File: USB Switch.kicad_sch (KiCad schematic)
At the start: 2 parts

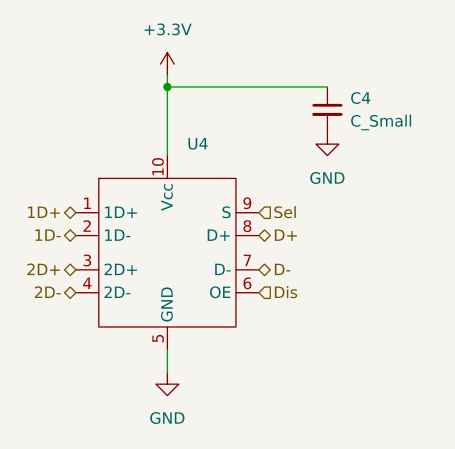
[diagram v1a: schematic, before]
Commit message: BMS updates
- BMS mostly done
- all BMS pins connected to RP2040
- Re-did Minibadge pinouts
- Connected RP2040 to USB Switch
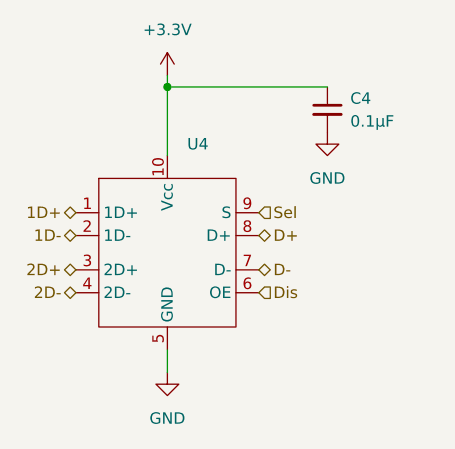
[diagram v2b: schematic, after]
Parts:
- C4: value C_Small -> 0.1μF
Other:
- company: (none) -> Pips Engineering
- title: (none) -> USB-C switch

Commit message: BMS updates
Added missing capacitor for OTG
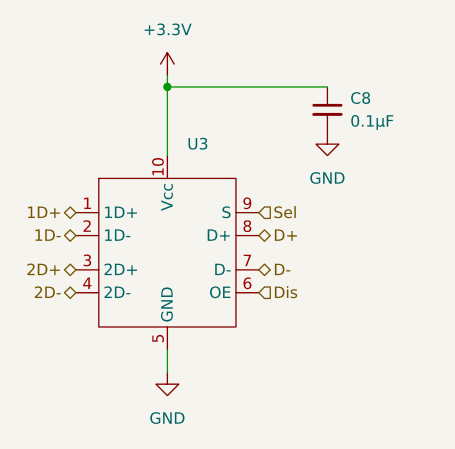
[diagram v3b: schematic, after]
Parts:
- renumbered C4 to C8, U4 to U3
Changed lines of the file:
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@@
 		(dnp no)
 		(fields_autoplaced yes)
-		(property "Reference" "#PWR0109"
+		(property "Reference" "#PWR026"
 			(at 162.56 81.28 0)
 			(effects
@@
 			(project "Minibadge Display 5x3"
 				(path "/e5119d15-74fb-4259-abbc-5cab1f368532/dd5131e2-5cc6-4770-9855-76714fa7cc76"
-					(reference "#PWR0109")
+					(reference "#PWR026")
 					(unit 1)
 				)
@@
 		(dnp no)
 		(fields_autoplaced yes)
-		(property "Reference" "#PWR0110"
+		(property "Reference" "#PWR025"
 			(at 144.78 107.95 0)
 			(effects
@@
 			(project ""
 				(path "/e5119d15-74fb-4259-abbc-5cab1f368532/dd5131e2-5cc6-4770-9855-76714fa7cc76"
-					(reference "#PWR0110")
+					(reference "#PWR025")
 					(unit 1)
 				)
@@
 		(dnp no)
 		(fields_autoplaced yes)
-		(property "Reference" "#PWR0108"
+		(property "Reference" "#PWR024"
 			(at 144.78 72.39 0)
 			(effects
@@
 			(project "Minibadge Display 5x3"
 				(path "/e5119d15-74fb-4259-abbc-5cab1f368532/dd5131e2-5cc6-4770-9855-76714fa7cc76"
-					(reference "#PWR0108")
+					(reference "#PWR024")
 					(unit 1)
 				)
@@
 		(dnp no)
 		(fields_autoplaced yes)
-		(property "Reference" "C4"
+		(property "Reference" "C8"
 			(at 165.1 71.1262 0)
 			(effects
@@
 			(project "Minibadge Display 5x3"
 				(path "/e5119d15-74fb-4259-abbc-5cab1f368532/dd5131e2-5cc6-4770-9855-76714fa7cc76"
-					(reference "C4")
+					(reference "C8")
 					(unit 1)
 				)
@@
 		(dnp no)
 		(fields_autoplaced yes)
-		(property "Reference" "U4"
+		(property "Reference" "U3"
 			(at 146.9741 76.2 0)
 			(effects
@@
 			(project "Minibadge Display 5x3"
 				(path "/e5119d15-74fb-4259-abbc-5cab1f368532/dd5131e2-5cc6-4770-9855-76714fa7cc76"
-					(reference "U4")
-					(unit 1)
-				)
+					(reference "U3")
+					(unit 1)
+				)
